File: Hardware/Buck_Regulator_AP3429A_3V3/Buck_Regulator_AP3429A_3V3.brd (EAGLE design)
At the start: 25.4 x 25.4 mm, 53 parts, among them J1 Screw Terminal, J2 POWER_JACKPOWER_JACK_SLOT_COM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, J3 Breakout Headers, U1 AP3429/A

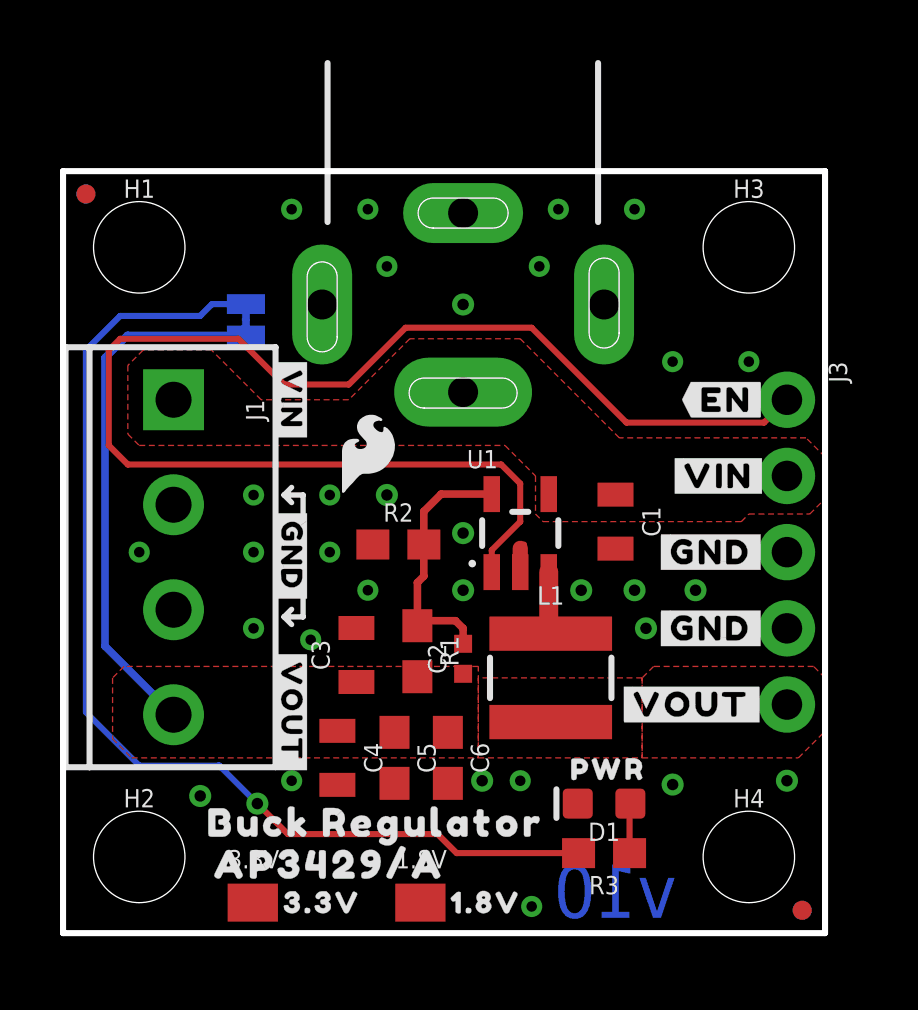
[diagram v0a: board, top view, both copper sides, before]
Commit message: Adjusted power jack for panelizing
There was an issue with overhanging silkscreen for the powerjack since the part is usually populated - the part is not populated for this specific part. This was changed from the device all the way through the panelized files.
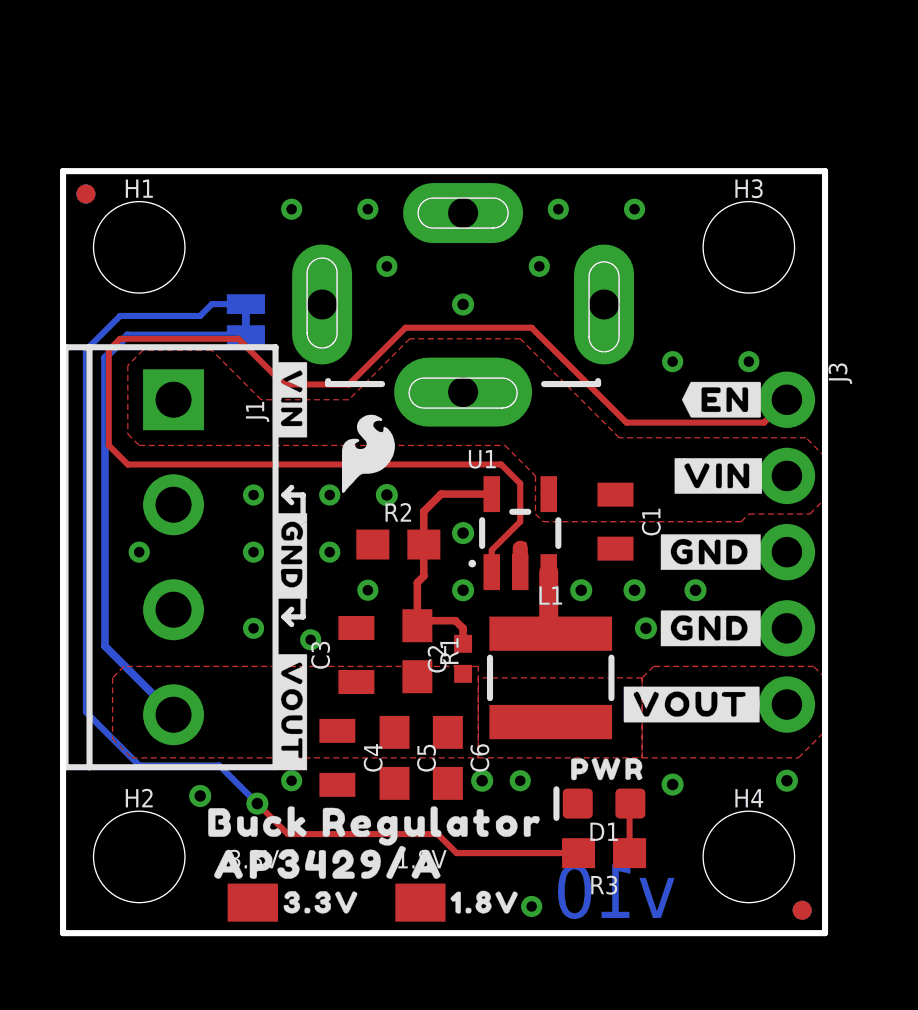
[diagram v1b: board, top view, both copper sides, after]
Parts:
- flipped J2 to the top
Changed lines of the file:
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@@
 <layer number="45" name="Holes" color="7" fill="1" visible="yes" active="yes"/>
 <layer number="46" name="Milling" color="3" fill="1" visible="no" active="yes"/>
-<layer number="47" name="Measures" color="7" fill="1" visible="yes" active="yes"/>
+<layer number="47" name="Measures" color="7" fill="1" visible="no" active="yes"/>
 <layer number="48" name="Document" color="7" fill="1" visible="no" active="yes"/>
 <layer number="49" name="Reference" color="7" fill="1" visible="no" active="yes"/>
@@
 <attribute name="VALUE" x="18.034" y="3.429" size="0.6096" layer="27" font="vector" ratio="20" rot="R180" align="top-center"/>
 </element>
-<element name="J2" library="SparkFun-Connectors" package="POWER_JACK_PTH_SLOT_BOTH" value="POWER_JACKPOWER_JACK_SLOT_COMBO" x="13.335" y="24.003" smashed="yes" rot="MR90"/>
 <element name="C5" library="SparkFun-Capacitors" package="0603" value="0.1uF" x="11.049" y="5.842" smashed="yes" rot="R270">
 <attribute name="NAME" x="11.811" y="5.842" size="0.6096" layer="25" font="vector" ratio="20" rot="R270" align="bottom-center"/>
@@
 <attribute name="VALUE" x="12.065" y="5.842" size="0.6096" layer="27" font="vector" ratio="20" rot="R270" align="top-center"/>
 </element>
+<element name="J2" library="SparkFun-Connectors" package="POWER_JACK_PTH_SLOT_BOTH" value="POWER_JACKPOWER_JACK_SLOT_COMBO" x="13.335" y="24.003" smashed="yes" rot="R90"/>
 </elements>
 <signals>
@@
 <via x="10.16" y="24.13" extent="1-16" drill="0.35"/>
 <contactref element="R2" pad="1"/>
-<contactref element="J2" pad="GND"/>
 <contactref element="C5" pad="2"/>
 <contactref element="C6" pad="2"/>
 <via x="13.97" y="5.08" extent="1-16" drill="0.381"/>
 <via x="4.572" y="4.572" extent="1-16" drill="0.381"/>
+<contactref element="J2" pad="GND"/>
 </signal>
 <signal name="N$1">

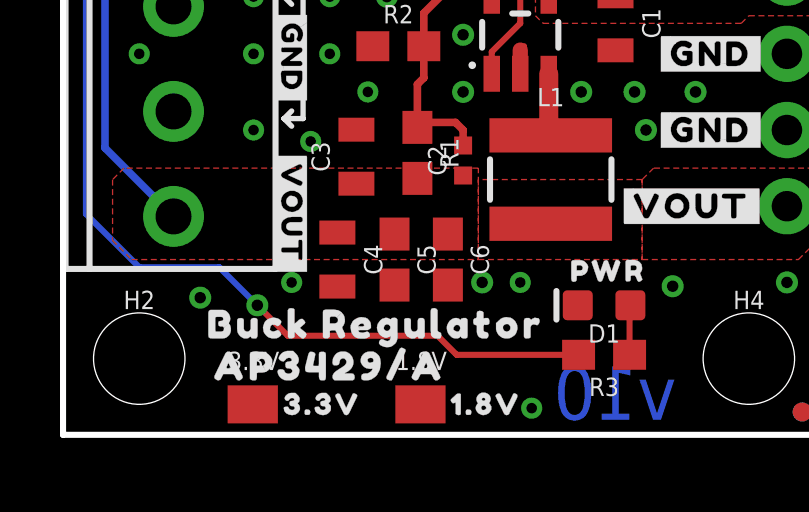
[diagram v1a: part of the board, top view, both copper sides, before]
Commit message: Updated panelized files
Adjusted via to no longer be in the way of the bStop on the back for the thermal pad on the backside. Included ordering instructions on the brd files for both 1.8V and 3.3V
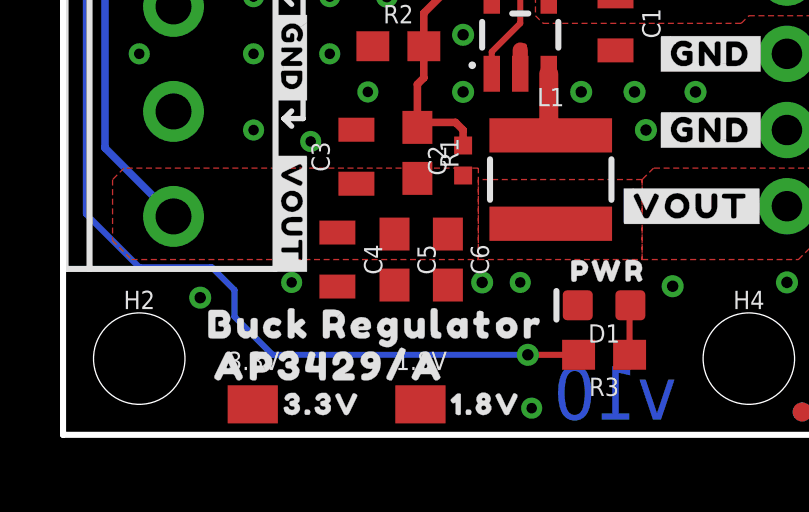
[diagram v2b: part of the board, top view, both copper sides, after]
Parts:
- added U$17: (no value), SparkFun-Aesthetics:ORDERING_INSTRUCTIONS
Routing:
- net N$3: track 36.4 -> 36.9 mm
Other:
- board text added: "Board thickness is 1.6mm 2-Layer 1oz copper outer 1oz copper inner"
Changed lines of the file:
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@@
 <dimension x1="13.335" y1="24.003" x2="13.335" y2="0" x3="-17.78" y3="12.0015" textsize="1.778" textratio="15" layer="47" unit="inch"/>
 <dimension x1="0" y1="25.4" x2="0" y2="0" x3="-21.59" y3="12.7" textsize="1.778" textratio="15" layer="47" unit="inch"/>
+<text x="33.528" y="4.699" size="1.778" layer="51" font="vector">Board thickness is 1.6mm
+2-Layer
+1oz copper outer
+1oz copper inner</text>
 </plain>
 <attributes>
@@
 </element>
 <element name="J2" library="SparkFun-Connectors" package="POWER_JACK_PTH_SLOT_BOTH" value="POWER_JACKPOWER_JACK_SLOT_COMBO" x="13.335" y="24.003" smashed="yes" rot="R90"/>
+<element name="U$17" library="SparkFun-Aesthetics" package="ORDERING_INSTRUCTIONS" value="" x="31.75" y="25.4" smashed="yes"/>
 </elements>
 <signals>
@@
 <wire x1="4.9657" y1="20.9677" x2="4.572" y2="20.574" width="0.2032" layer="16"/>
 <wire x1="4.572" y1="20.574" x2="1.905" y2="20.574" width="0.2032" layer="16"/>
-<wire x1="12.485" y1="3.302" x2="13.12" y2="2.667" width="0.2032" layer="1"/>
-<wire x1="12.485" y1="3.302" x2="7.493" y2="3.302" width="0.2032" layer="1"/>
-<via x="6.477" y="4.318" extent="1-16" drill="0.381"/>
-<wire x1="6.477" y1="4.318" x2="7.493" y2="3.302" width="0.2032" layer="1"/>
 <wire x1="0.762" y1="19.431" x2="0.762" y2="7.366" width="0.2032" layer="16"/>
 <wire x1="0.762" y1="7.366" x2="2.54" y2="5.588" width="0.2032" layer="16"/>
-<wire x1="5.207" y1="5.588" x2="6.477" y2="4.318" width="0.2032" layer="16"/>
-<wire x1="5.207" y1="5.588" x2="2.54" y2="5.588" width="0.2032" layer="16"/>
 <contactref element="R3" pad="2"/>
-<wire x1="13.12" y1="2.667" x2="17.184" y2="2.667" width="0.2032" layer="1"/>
+<via x="15.494" y="2.667" extent="1-16" drill="0.381"/>
+<wire x1="15.494" y1="2.667" x2="17.184" y2="2.667" width="0.2032" layer="1"/>
+<wire x1="5.715" y1="4.826" x2="5.715" y2="3.937" width="0.2032" layer="16"/>
+<wire x1="5.715" y1="3.937" x2="6.985" y2="2.667" width="0.2032" layer="16"/>
+<wire x1="2.54" y1="5.588" x2="4.953" y2="5.588" width="0.2032" layer="16"/>
+<wire x1="4.953" y1="5.588" x2="5.715" y2="4.826" width="0.2032" layer="16"/>
+<wire x1="6.985" y1="2.667" x2="15.494" y2="2.667" width="0.2032" layer="16"/>
 </signal>
 <signal name="N$4">
@@
 </drawing>
 <compatibility>
+<note version="6.3" minversion="6.2.2" severity="warning">
+Since Version 6.2.2 text objects can contain more than one line,
+which will not be processed correctly with this version.
+</note>
 <note version="8.3" severity="warning">
 Since Version 8.3, EAGLE supports URNs for individual library
